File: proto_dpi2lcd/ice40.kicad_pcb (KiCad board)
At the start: 4 copper layers, 50 x 50 mm, 61 parts, among them J101 Conn_01x40_MountingPin, J102 Raspberry_Pi_2_3, J103 Conn_02x05_Odd_Even, J201 Barrel_Jack_Switch, SW101 SW1, SW102 SW2, U101 iCE40HX1K-CB132, U102 W25Q32JVSS, U103 520-2520MVLC-400BNTR, U201 TLV71325PDBV, U202 ST1S10PHR, U203 TLV71312PDBV

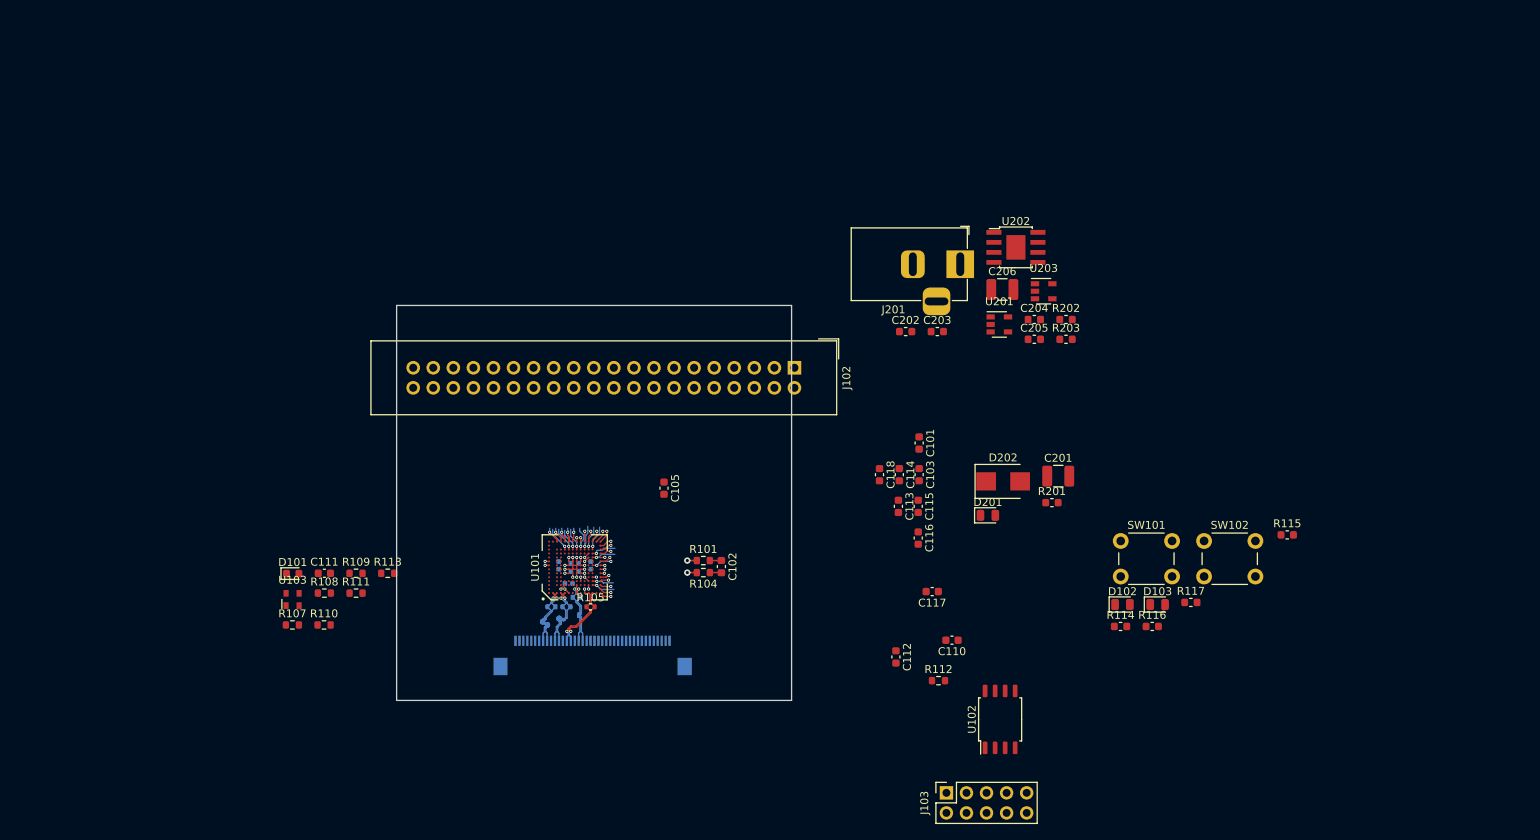
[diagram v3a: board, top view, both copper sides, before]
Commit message: Progress
Sheets work
 - almost all J101 singals connected with FPGA
 - Bank IOT connected to +2V5
 - bus added between J101 and FPGA
 - general sheet cleanup
 - LEDs and SWs connected to FPGA

PCB work:
 - J101 aligned
 - push buttons and LEDs aligned
 - more fanout to the FPGA

And some other things for sure.
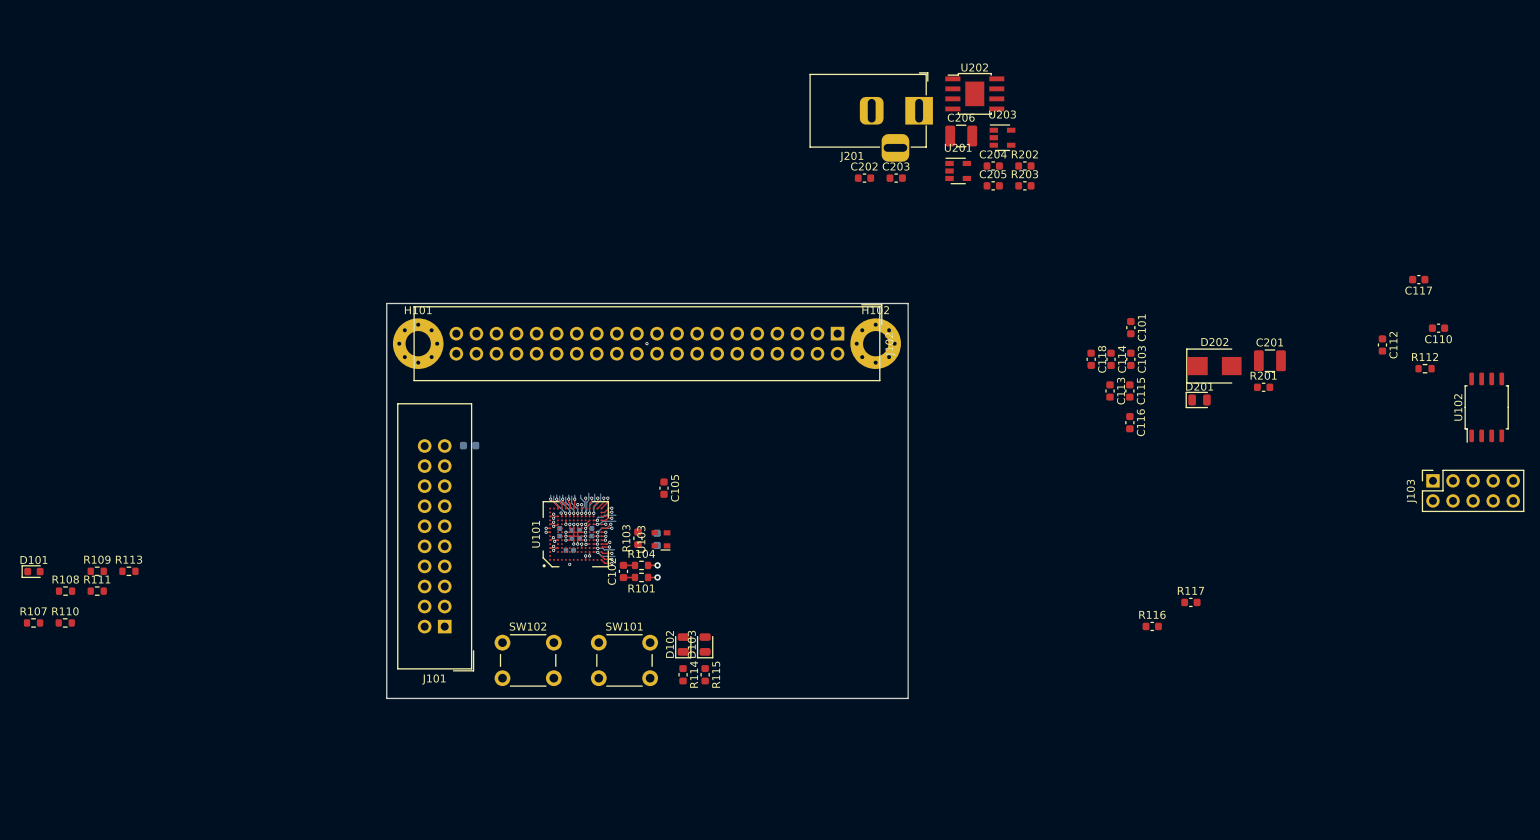
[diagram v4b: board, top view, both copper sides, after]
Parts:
- removed R105, R106: 100R 1%, Resistor_SMD:R_0402_1005Metric
- added H101: MountingHole_Pad, MountingHole:MountingHole_3.2mm_M3_Pad_Via, F.Cu at (126.0, 85.1)
- added H102: MountingHole_Pad, MountingHole:MountingHole_3.2mm_M3_Pad_Via, F.Cu at (183.9, 85.1)
- C111: moved to B.Cu
- J101: value Conn_01x40_MountingPin -> TFT_LCD_MODULE; footprint Connector_FFC-FPC:Hirose_FH12-40S-0.5SH_1x40-1MP_P0.50mm_Horizontal -> Connector_IDC:IDC-Header_2x10_P2.54mm_Vertical; moved to F.Cu
- R102: value 100R 1% -> NM; footprint Resistor_SMD:R_0402_1005Metric -> Resistor_SMD:R_0603_1608Metric
- R103: value 100R 1% -> 22R; footprint Resistor_SMD:R_0402_1005Metric -> Resistor_SMD:R_0603_1608Metric; moved to F.Cu
- R114, R115: value 200R -> 470R
- moved SW102 89.7 mm to (136.7, 122.9)
- moved R115 75.8 mm to (162.3, 127.0), turned to 270 degrees
- moved C110 73.2 mm to (255.2, 83.1)
- moved C112 73.2 mm to (248.1, 85.3)
- moved C117 73.2 mm to (252.7, 77.0)
- moved J103 73.2 mm to (254.4, 102.5)
- moved R112 73.2 mm to (253.4, 88.3)
- moved U102 73.2 mm to (261.2, 93.2)
- moved SW101 67.3 mm to (148.8, 122.9)
- moved D103 57.5 mm to (162.3, 123.2), turned to 90 degrees
- moved D102 55.8 mm to (159.5, 123.2), turned to 90 degrees
- moved R114 55.7 mm to (159.5, 127.0), turned to 270 degrees
- moved U103 47.3 mm to (156.7, 109.9), turned to 90 degrees
- moved C111 42.3 mm to (156.2, 109.9), turned to 270 degrees
- moved R107 32.8 mm to (77.3, 120.4)
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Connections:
- C117 pad 2: +3V3 -> +2V5
- C118 pad 2: +3V3 -> +2V5
- D102 pad 1: GND -> Net-(D102-Pad1)
- D102 pad 2: Net-(D102-Pad2) -> /LED1
- D103 pad 1: GND -> Net-(D103-Pad1)
- D103 pad 2: Net-(D103-Pad2) -> /LED2
- J101 pad 1: /LED_VCCS -> /lcd_VCC
- J101 pad 10: GNDPWR -> GND
- J101 pad 11: (no net) -> /RXout2_N
- J101 pad 12: (no net) -> /RXout2_P
- J101 pad 14: (no net) -> /RxoutC_N
- J101 pad 15: (no net) -> /RxoutC_P
- J101 pad 17: (no net) -> /RXout3_N
- J101 pad 18: (no net) -> /RXout3_P
- J101 pad 19: GND -> /RSV
- J101 pad 2: /LED_VCCS -> /lcd_VCC
- J101 pad 20: (no net) -> /SEL68
- J101 pad 3: /LED_VCCS -> GND
- J101 pad 4: (no net) -> /DPS
- J101 pad 5: (no net) -> /RXout0_N
- J101 pad 6: (no net) -> /RXout0_P
- J101 pad 7: (no net) -> GND
- J101 pad 8: GNDPWR -> /RXout1_N
- J101 pad 9: GNDPWR -> /RXout1_P
- R102 pad 1: /Rxin0- -> /RSV
- R102 pad 2: /Rxin0+ -> GND
- R103 pad 1: /Rxin1- -> /CLOCK
- R103 pad 2: /Rxin1+ -> Net-(R103-Pad2)
- R114 pad 1: (no net) -> Net-(D102-Pad1)
- R114 pad 2: Net-(D102-Pad2) -> GND
- R115 pad 1: (no net) -> Net-(D103-Pad1)
- R115 pad 2: Net-(D103-Pad2) -> GND
- U101 pad A1: (no net) -> /RXout0_P
- U101 pad A10: (no net) -> /RxoutC_N
- U101 pad A12: (no net) -> /RXout3_P
- U101 pad A2: (no net) -> /RXout0_N
- U101 pad A4: (no net) -> /RXout1_P
- U101 pad A5: (no net) -> /SW1
- U101 pad A6: (no net) -> /RXout2_P
- U101 pad A7: (no net) -> /SW2
- U101 pad A8: +3V3 -> +2V5
- U101 pad B1: /Rxin0- -> (no net)
- U101 pad C1: /Rxin0+ -> (no net)
- U101 pad C10: (no net) -> /RxoutC_P
- U101 pad C12: (no net) -> /RXout3_N
- U101 pad C4: (no net) -> /RXout1_N
- U101 pad C6: (no net) -> /RXout2_N
- U101 pad D1: /Rxin1- -> (no net)
- U101 pad D12: (no net) -> /SEL68
- U101 pad E1: /Rxin1+ -> (no net)
- U101 pad E11: (no net) -> /DPS
- U101 pad F6: +3V3 -> +2V5
- U101 pad H1: /RxCLK+ -> (no net)
- U101 pad H3: /RxCLK- -> (no net)
- U101 pad L1: /Rxin2- -> (no net)
- U101 pad L5: (no net) -> /LED1
- U101 pad M1: /Rxin2+ -> (no net)
- U101 pad M6: (no net) -> /LED2
- U101 pad M7: (no net) -> /G6
- U101 pad P7: /G6 -> /CLOCK
- U103 pad 3: (no net) -> Net-(R103-Pad2)
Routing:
- net /Rxin0+: track 8.55 -> 0.00 mm, vias 1 -> 0
- net /Rxin1-: track 8.50 -> 0.00 mm, vias 1 -> 0
- net /Rxin0-: track 8.42 -> 0.00 mm, vias 1 -> 0
- net /Rxin1+: track 8.37 -> 0.00 mm, vias 1 -> 0
- net /RxCLK-: track 8.26 -> 0.00 mm, vias 1 -> 0
- net /RxCLK+: track 8.26 -> 0.00 mm, vias 1 -> 0
- net /Rxin2+: track 8.18 -> 0.00 mm, vias 1 -> 0
- net /Rxin2-: track 8.18 -> 0.00 mm, vias 1 -> 0
- net +3V3: track 4.92 -> 3.92 mm, vias 8 -> 6
- net GND: track 9.91 -> 9.21 mm
- net (no net): track 2.24 -> 1.54 mm
- net /RXout1_N: track 0.00 -> 0.67 mm, vias 0 -> 1
- net /RxoutC_P: track 0.00 -> 0.65 mm, vias 0 -> 1
- net /RXout3_N: track 0.00 -> 0.64 mm, vias 0 -> 1
- net /RXout3_P: track 0.00 -> 0.57 mm, vias 0 -> 1
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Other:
- board size 50 x 50 mm -> 66 x 50 mm

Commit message: Work in progress
- Added BUCK for 12V->5V but inductors are TBD
 - Progress to the layout
 - some pin swapping has been done
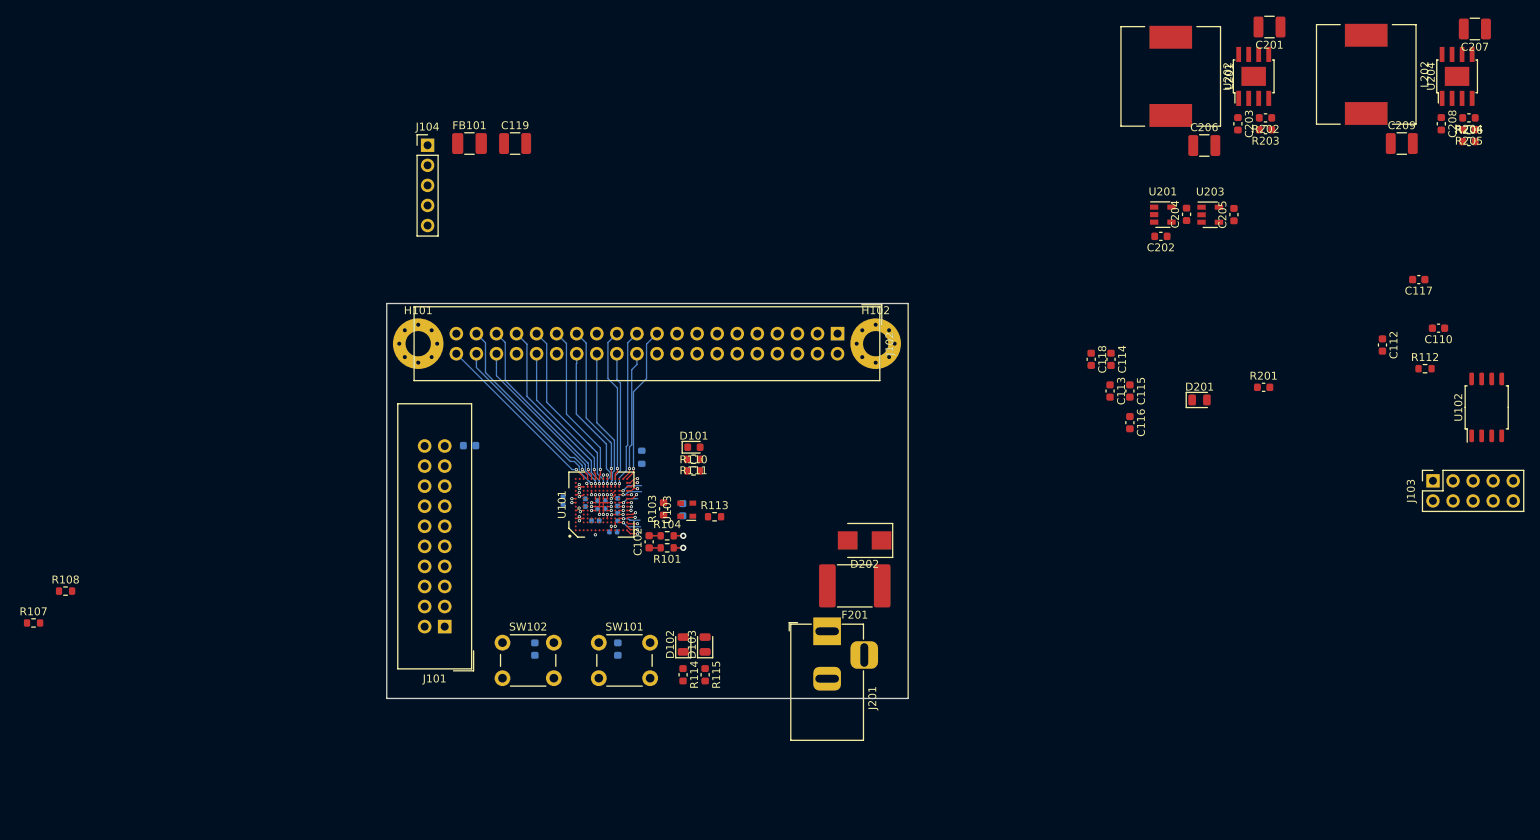
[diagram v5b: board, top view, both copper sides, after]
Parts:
- added C119: 22u/25V, Capacitor_SMD:C_1210_3225Metric, F.Cu at (138.2, 59.8)
- added C207: 10u/35V, Capacitor_SMD:C_1210_3225Metric, F.Cu at (259.8, 45.2)
- added C208: 100n, Capacitor_SMD:C_0603_1608Metric, F.Cu at (255.5, 57.2)
- added C209: 22u/25V, Capacitor_SMD:C_1210_3225Metric, F.Cu at (250.5, 59.8)
- added F201: SL200-16, Fuse:Fuse_2920_7451Metric_Pad2.10x5.45mm_HandSolder, F.Cu at (181.2, 115.8)
- added FB101: Ferrite_Bead_Small, Inductor_SMD:L_1210_3225Metric_Pad1.42x2.65mm_HandSolder, F.Cu at (132.5, 59.8)
- added J104: LCD_BACKLIGHT, Connector_PinHeader_2.54mm:PinHeader_1x05_P2.54mm_Vertical, F.Cu at (127.2, 60.0)
- added L201: 4u7, Inductor_SMD:L_12x12mm_H8mm, F.Cu at (221.2, 51.2)
- added L202: 4u7, Inductor_SMD:L_12x12mm_H8mm, F.Cu at (246.0, 51.0)
- added R204: 10k, Resistor_SMD:R_0603_1608Metric, F.Cu at (259.0, 56.5)
- added R205: 27k, Resistor_SMD:R_0603_1608Metric, F.Cu at (259.0, 58.0)
- added R206: 27k, Resistor_SMD:R_0603_1608Metric, F.Cu at (259.0, 59.5)
- added U204: ST1S10PHR, Package_SO:TI_SO-PowerPAD-8, F.Cu at (257.5, 51.2)
- C101, C103, C105: footprint Capacitor_SMD:C_0603_1608Metric -> Capacitor_SMD:C_0402_1005Metric; moved to B.Cu
- R109, R116, R117: moved to B.Cu
- moved D101 85.0 mm to (160.9, 98.2)
- moved R117 83.3 mm to (140.8, 123.8), turned to 90 degrees
- moved R110 81.8 mm to (160.8, 101.2)
- moved R111 77.3 mm to (160.8, 99.7), turned to 180 degrees
- moved C101 75.1 mm to (144.3, 105.0)
- moved R113 74.5 mm to (163.5, 107.0)
- moved R109 70.4 mm to (154.3, 99.5), turned to 90 degrees
- moved C103 69.1 mm to (150.7, 108.9), turned to 180 degrees
- moved R116 67.7 mm to (151.2, 123.8), turned to 90 degrees
- moved J201 66.9 mm to (177.8, 121.5), turned to 90 degrees
- moved D202 49.5 mm to (182.5, 110.0), turned to 180 degrees
- moved C203 43.8 mm to (229.8, 57.2), turned to 270 degrees
- moved C201 42.2 mm to (233.8, 45.0), turned to 180 degrees
- moved C202 38.2 mm to (220.0, 71.5), turned to 180 degrees
- moved U202 35.4 mm to (231.8, 51.2), turned to 90 degrees
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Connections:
- J201 pad 1: +12V -> Net-(F201-Pad2)
- U101 pad B14: (no net) -> /BL_EN
- U101 pad D14: /R0 -> /R6
- U101 pad E12: /R6 -> /R0
- U101 pad E14: /G4 -> /G7
- U101 pad F12: /G7 -> /G4
- U101 pad F14: /G1 -> /G0
- U101 pad G12: /G0 -> /G1
- U101 pad G14: /B2 -> /B1
- U101 pad H12: /B1 -> /B2
- U101 pad K12: /CLK -> /B3
- U101 pad K14: /B3 -> /CLK
- U101 pad M12: /R5 -> /B5
- U101 pad M9: (no net) -> /BL_ADJ
- U101 pad N14: /B5 -> /R5
- U202 pad 7: (no net) -> Net-(L201-Pad1)
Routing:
- net /B2: track 1.74 -> 23.6 mm
- net /G1: track 2.28 -> 23.7 mm
- net /R6: track 3.21 -> 24.5 mm
- net /R0: track 1.97 -> 23.2 mm
- net /R1: track 2.08 -> 22.8 mm
- net /G7: track 3.11 -> 23.4 mm
- net /G4: track 1.89 -> 22.1 mm
- net /B5: track 1.64 -> 20.3 mm
- net /B6: track 1.65 -> 20.0 mm
- net /B7: track 1.43 -> 19.5 mm
- net /B1: track 2.88 -> 20.7 mm
- net /CLK: track 3.11 -> 20.2 mm
- net /B3: track 1.32 -> 17.9 mm
- net /G0: track 2.86 -> 19.5 mm
- net /DEN: track 3.06 -> 18.8 mm
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
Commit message: 1st routing of the rpi connector
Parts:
- C111: moved to F.Cu
- moved C111 1.81 mm to (160.0, 107.8), turned to 180 degrees
- moved C107 0.58 mm to (147.2, 105.8)
- moved U103 0.57 mm to (160.0, 105.5)
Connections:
- U101 pad M3: /B0 -> /H_SYNC
- U101 pad M4: /G3 -> /B0
- U101 pad M7: /G6 -> /G5
- U101 pad P3: /H_SYNC -> /G2
- U101 pad P4: /G2 -> /G3
- U101 pad P5: /G5 -> /G6
- U101 pad P8: /R2 -> /R3
- U101 pad P9: /R3 -> /R2
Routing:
- net /V_SYNC: track 1.50 -> 39.6 mm
- net /H_SYNC: track 1.39 -> 39.2 mm
- net /B0: track 2.93 -> 37.6 mm
- net /G2: track 1.08 -> 35.0 mm
- net /G5: track 1.16 -> 32.1 mm
- net /G6: track 0.55 -> 29.1 mm
- net /G3: track 2.73 -> 31.0 mm
- net /R7: track 2.53 -> 29.9 mm
- net /R2: track 0.56 -> 26.4 mm
- net /R3: track 1.40 -> 26.0 mm
- net /R4: track 0.56 -> 22.2 mm
- net /CRESET: track 0.71 -> 4.12 mm
- net /LED2: track 0.52 -> 2.34 mm
- net /CLOCK: track 0.55 -> 1.86 mm
- net Net-(C102-Pad2): track 2.97 -> 3.87 mm

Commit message: Routing progress
- switched to KiCAD 6.0.0
 - defined stackup, according to JLC PCB inside the project PCB settings
 - fully routed FGPA to 40pin header, with track length tunned
 - routed diff-pairs of LVDSes from FPGA to the pin-header
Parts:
- moved R107 97.8 mm to (173.9, 105.4)
- moved R108 89.9 mm to (170.5, 105.4)
- moved C111 8.78 mm to (163.3, 116.0)
- moved R113 8.78 mm to (166.7, 115.2)
- moved U103 8.78 mm to (163.3, 113.7)
- moved R103 8.53 mm to (160.7, 113.7)
- moved R104 5.06 mm to (154.0, 113.1), turned to 180 degrees
- moved C101 4.78 mm to (149.1, 105.1)
- moved R109 4.73 mm to (159.0, 99.6)
- moved R102 4.57 mm to (128.5, 95.8), turned to 180 degrees
- moved C104 4.52 mm to (155.8, 105.2)
- moved C105 4.52 mm to (155.8, 107.1)
- moved U101 4.52 mm to (153.7, 105.5)
- moved C103 4.52 mm to (155.2, 109.0)
- moved C106 4.52 mm to (153.7, 105.0)
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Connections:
- J102 pad 1: (no net) -> unconnected-(J102-Pad1)
- J102 pad 10: /G3 -> /B0
- J102 pad 17: (no net) -> unconnected-(J102-Pad17)
- J102 pad 2: (no net) -> unconnected-(J102-Pad2)
- J102 pad 4: (no net) -> unconnected-(J102-Pad4)
- J102 pad 7: /B0 -> /G3
- J103 pad 3: (no net) -> unconnected-(J103-Pad3)
- J103 pad 4: (no net) -> unconnected-(J103-Pad4)
- J104 pad 5: (no net) -> unconnected-(J104-Pad5)
- J201 pad 3: (no net) -> unconnected-(J201-Pad3)
- U101 pad A11: (no net) -> unconnected-(U101-PadA11)
- U101 pad A13: (no net) -> unconnected-(U101-PadA13)
- U101 pad A3: (no net) -> unconnected-(U101-PadA3)
- U101 pad B1: (no net) -> /Rxin0-
- U101 pad C1: (no net) -> /Rxin0+
- U101 pad C11: (no net) -> unconnected-(U101-PadC11)
- U101 pad C3: (no net) -> unconnected-(U101-PadC3)
- U101 pad C5: (no net) -> unconnected-(U101-PadC5)
- U101 pad C7: (no net) -> unconnected-(U101-PadC7)
- U101 pad C8: (no net) -> unconnected-(U101-PadC8)
- U101 pad C9: (no net) -> unconnected-(U101-PadC9)
- U101 pad D1: (no net) -> /Rxin1-
- U101 pad D10: (no net) -> unconnected-(U101-PadD10)
- U101 pad D11: (no net) -> unconnected-(U101-PadD11)
- U101 pad D3: (no net) -> unconnected-(U101-PadD3)
- U101 pad D4: (no net) -> unconnected-(U101-PadD4)
- U101 pad D5: (no net) -> unconnected-(U101-PadD5)
- U101 pad D6: (no net) -> unconnected-(U101-PadD6)
- U101 pad D7: (no net) -> unconnected-(U101-PadD7)
- U101 pad D8: (no net) -> unconnected-(U101-PadD8)
- U101 pad D9: (no net) -> unconnected-(U101-PadD9)
- U101 pad E1: (no net) -> /Rxin1+
- U101 pad E4: (no net) -> unconnected-(U101-PadE4)
- U101 pad F11: (no net) -> unconnected-(U101-PadF11)
- U101 pad F3: (no net) -> unconnected-(U101-PadF3)
- U101 pad F4: (no net) -> unconnected-(U101-PadF4)
- U101 pad G1: (no net) -> unconnected-(U101-PadG1)
- U101 pad G11: (no net) -> unconnected-(U101-PadG11)
- U101 pad G3: (no net) -> unconnected-(U101-PadG3)
- U101 pad G4: (no net) -> unconnected-(U101-PadG4)
- U101 pad H1: (no net) -> /RxCLK+
- U101 pad H11: (no net) -> unconnected-(U101-PadH11)
- U101 pad H3: (no net) -> /RxCLK-
- U101 pad H4: (no net) -> unconnected-(U101-PadH4)
- U101 pad J1: (no net) -> unconnected-(U101-PadJ1)
- U101 pad J11: (no net) -> unconnected-(U101-PadJ11)
- U101 pad J3: (no net) -> unconnected-(U101-PadJ3)
- U101 pad K11: (no net) -> unconnected-(U101-PadK11)
- U101 pad K3: (no net) -> unconnected-(U101-PadK3)
- U101 pad K4: (no net) -> unconnected-(U101-PadK4)
- U101 pad L1: (no net) -> /Rxin2-
- U101 pad L4: (no net) -> unconnected-(U101-PadL4)
- U101 pad L6: (no net) -> unconnected-(U101-PadL6)
- U101 pad L7: (no net) -> unconnected-(U101-PadL7)
- U101 pad L8: (no net) -> unconnected-(U101-PadL8)
- U101 pad L9: (no net) -> unconnected-(U101-PadL9)
- U101 pad M1: (no net) -> /Rxin2+
- U101 pad M14: (no net) -> unconnected-(U101-PadM14)
- U101 pad M3: /H_SYNC -> /LED2
- U101 pad M4: /B0 -> /G3
- U101 pad M6: /LED2 -> /G6
- U101 pad P3: /G2 -> /H_SYNC
- U101 pad P4: /G3 -> /G2
- U101 pad P5: /G6 -> /B0
- U201 pad 4: (no net) -> unconnected-(U201-Pad4)
- U203 pad 4: (no net) -> unconnected-(U203-Pad4)
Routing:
- net /RXout0_P: track 0.00 -> 30.1 mm, vias 0 -> 1
- net /RXout0_N: track 0.00 -> 29.6 mm, vias 0 -> 1
- net /RxoutC_P: track 0.65 -> 28.8 mm
- net /RxoutC_N: track 0.56 -> 28.6 mm
- net /RXout1_P: track 0.54 -> 27.7 mm
- net /RXout3_P: track 0.57 -> 27.2 mm
- net /RXout1_N: track 0.67 -> 27.3 mm
- net /RXout3_N: track 0.64 -> 27.1 mm
- net /RXout2_P: track 0.55 -> 26.0 mm
- net /RXout2_N: track 0.48 -> 25.6 mm
- net /R5: track 16.6 -> 36.4 mm
- net /B4: track 17.3 -> 36.5 mm
- net /B3: track 17.9 -> 36.5 mm
- net /DEN: track 18.8 -> 36.4 mm
- net /G0: track 19.5 -> 37.0 mm
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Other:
- net class Default removed
- net class Diff100 removed
